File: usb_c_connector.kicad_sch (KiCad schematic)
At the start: 18 parts, among them J5 USB_C_Receptacle_USB2.0_16P, J6 USB_C_Receptacle_USB2.0_16P, U8 USBLC6-2SC6, U9 USBLC6-2SC6

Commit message: Use basic parts where possible
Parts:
- C26, C27, C28, C29, C30, C31: footprint Capacitor_SMD:C_0603_1608Metric_Pad1.08x0.95mm_HandSolder -> Capacitor_SMD:C_0603_1608Metric
- R13, R15, R31, R32: footprint Resistor_SMD:R_0603_1608Metric_Pad0.98x0.95mm_HandSolder -> Resistor_SMD:R_0603_1608Metric; LCSC PN C105580 -> C23186
- R17, R18: footprint Resistor_SMD:R_0603_1608Metric_Pad0.98x0.95mm_HandSolder -> Resistor_SMD:R_0603_1608Metric; LCSC PN C105578 -> C22935
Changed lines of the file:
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@@
 			)
 		)
-		(property "Footprint" "Resistor_SMD:R_0603_1608Metric_Pad0.98x0.95mm_HandSolder"
+		(property "Footprint" "Resistor_SMD:R_0603_1608Metric"
 			(at 86.36 80.518 90)
 			(effects
@@
 			)
 		)
-		(property "LCSC PN" "C105580"
+		(property "LCSC PN" "C23186"
 			(at 86.36 78.74 90)
 			(effects
@@
 			)
 		)
-		(property "Footprint" "Capacitor_SMD:C_0603_1608Metric_Pad1.08x0.95mm_HandSolder"
+		(property "Footprint" "Capacitor_SMD:C_0603_1608Metric"
 			(at 248.6152 78.74 0)
 			(effects
@@
 			)
 		)
-		(property "Footprint" "Resistor_SMD:R_0603_1608Metric_Pad0.98x0.95mm_HandSolder"
+		(property "Footprint" "Resistor_SMD:R_0603_1608Metric"
 			(at 198.12 83.058 90)
 			(effects
@@
 			)
 		)
-		(property "LCSC PN" "C105580"
+		(property "LCSC PN" "C23186"
 			(at 198.12 81.28 90)
 			(effects
@@
 			)
 		)
-		(property "Footprint" "Capacitor_SMD:C_0603_1608Metric_Pad1.08x0.95mm_HandSolder"
+		(property "Footprint" "Capacitor_SMD:C_0603_1608Metric"
 			(at 165.4048 121.92 0)
 			(effects
@@
 			)
 		)
-		(property "Footprint" "Capacitor_SMD:C_0603_1608Metric_Pad1.08x0.95mm_HandSolder"
+		(property "Footprint" "Capacitor_SMD:C_0603_1608Metric"
 			(at 234.6452 78.74 0)
 			(effects
@@
 			)
 		)
-		(property "Footprint" "Resistor_SMD:R_0603_1608Metric_Pad0.98x0.95mm_HandSolder"
+		(property "Footprint" "Resistor_SMD:R_0603_1608Metric"
 			(at 198.12 80.518 90)
 			(effects
@@
 			)
 		)
-		(property "LCSC PN" "C105580"
+		(property "LCSC PN" "C23186"
 			(at 198.12 78.74 90)
 			(effects
@@
 			)
 		)
-		(property "Footprint" "Capacitor_SMD:C_0603_1608Metric_Pad1.08x0.95mm_HandSolder"
+		(property "Footprint" "Capacitor_SMD:C_0603_1608Metric"
 			(at 53.6448 121.92 0)
 			(effects
@@
 			)
 		)
-		(property "Footprint" "Resistor_SMD:R_0603_1608Metric_Pad0.98x0.95mm_HandSolder"
+		(property "Footprint" "Resistor_SMD:R_0603_1608Metric"
 			(at 86.36 83.058 90)
 			(effects
@@
 			)
 		)
-		(property "LCSC PN" "C105580"
+		(property "LCSC PN" "C23186"
 			(at 86.36 81.28 90)
 			(effects
@@
 			)
 		)
-		(property "Footprint" "Resistor_SMD:R_0603_1608Metric_Pad0.98x0.95mm_HandSolder"
+		(property "Footprint" "Resistor_SMD:R_0603_1608Metric"
 			(at 173.228 118.11 90)
 			(effects
@@
 			)
 		)
-		(property "LCSC PN" "C105578"
+		(property "LCSC PN" "C22935"
 			(at 171.45 118.11 0)
 			(effects
@@
 			)
 		)
-		(property "Footprint" "Resistor_SMD:R_0603_1608Metric_Pad0.98x0.95mm_HandSolder"
+		(property "Footprint" "Resistor_SMD:R_0603_1608Metric"
 			(at 61.468 118.11 90)
 			(effects
@@
 			)
 		)
-		(property "LCSC PN" "C105578"
+		(property "LCSC PN" "C22935"
 			(at 59.69 118.11 0)
 			(effects
@@
 			)
 		)
-		(property "Footprint" "Capacitor_SMD:C_0603_1608Metric_Pad1.08x0.95mm_HandSolder"
+		(property "Footprint" "Capacitor_SMD:C_0603_1608Metric"
 			(at 136.8552 78.74 0)
 			(effects
@@
 			)
 		)
-		(property "Footprint" "Capacitor_SMD:C_0603_1608Metric_Pad1.08x0.95mm_HandSolder"
+		(property "Footprint" "Capacitor_SMD:C_0603_1608Metric"
 			(at 122.8852 78.74 0)
 			(effects

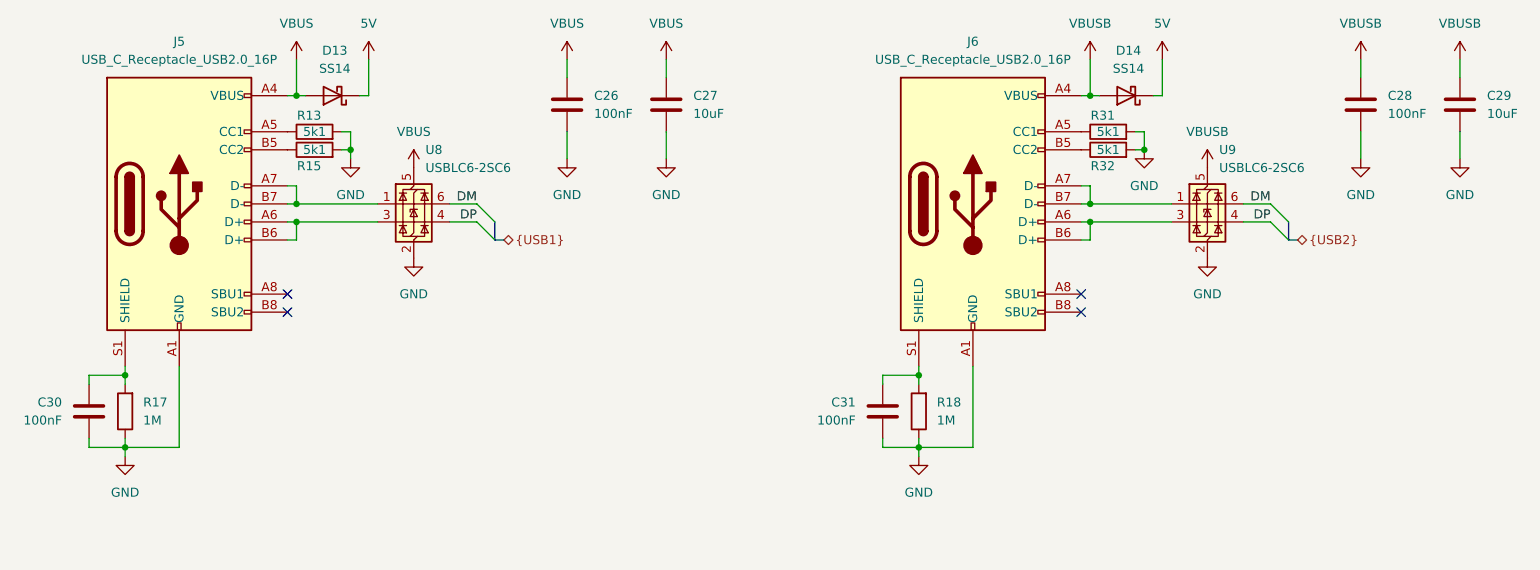
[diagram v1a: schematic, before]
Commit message: Fix bus merging and add net classes
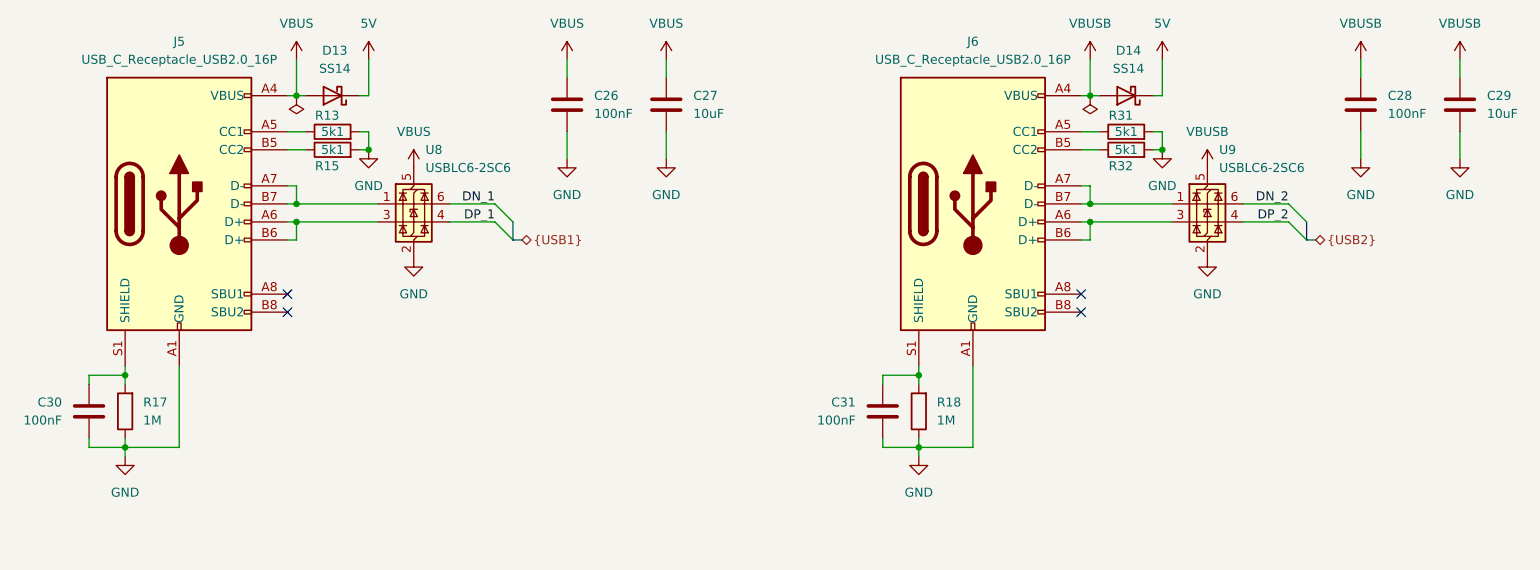
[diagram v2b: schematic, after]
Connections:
- net DM renamed DN_1
- net DN_1: no longer U9.6 (I/O1)
- net DP renamed DP_1
- net DP_1: no longer U9.4 (I/O2)
- new net DN_2: U9.6 (I/O1)
- new net DP_2: U9.4 (I/O2)
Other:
- moved on the sheet: R13, R15, R31, R32

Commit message: Continue layout and update schematic
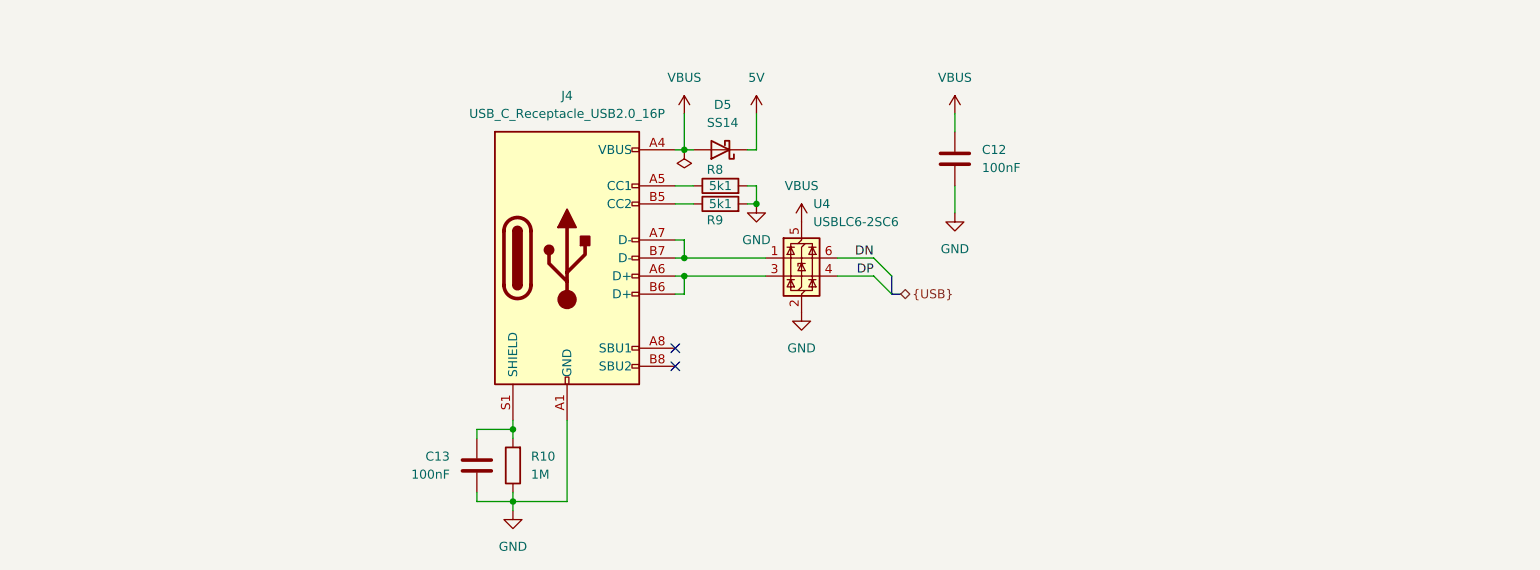
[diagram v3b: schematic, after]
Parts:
- removed C27, C29: 10uF, Capacitor_SMD:C_0603_1608Metric, symbol Device:C
- removed C28, C31: 100nF, Capacitor_SMD:C_0603_1608Metric, symbol Device:C
- removed D14: SS14, Diode_SMD:D_SMA, symbol Diode:SS14
- removed J6: USB_C_Receptacle_USB2.0_16P, Tumbler2:KINGHELM_KH-TYPE-C-16P, symbol Connector:USB_C_Receptacle_USB2.0_16P
- removed R18: 1M, Resistor_SMD:R_0603_1608Metric, symbol Device:R
- removed R31, R32: 5k1, Resistor_SMD:R_0603_1608Metric, symbol Device:R
- removed U9: USBLC6-2SC6, Package_TO_SOT_SMD:SOT-23-6, symbol Power_Protection:USBLC6-2SC6
- renumbered C26 to C12, C30 to C13, D13 to D5, J5 to J4, R17 to R10, R13 to R8, R15 to R9, U8 to U4
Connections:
- net DN_1 renamed DN
- net DP_1 renamed DP
- no-connect marks 4 -> 2
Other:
- moved on the sheet: C12, C13, D5, J4, R10, R8, R9, U4

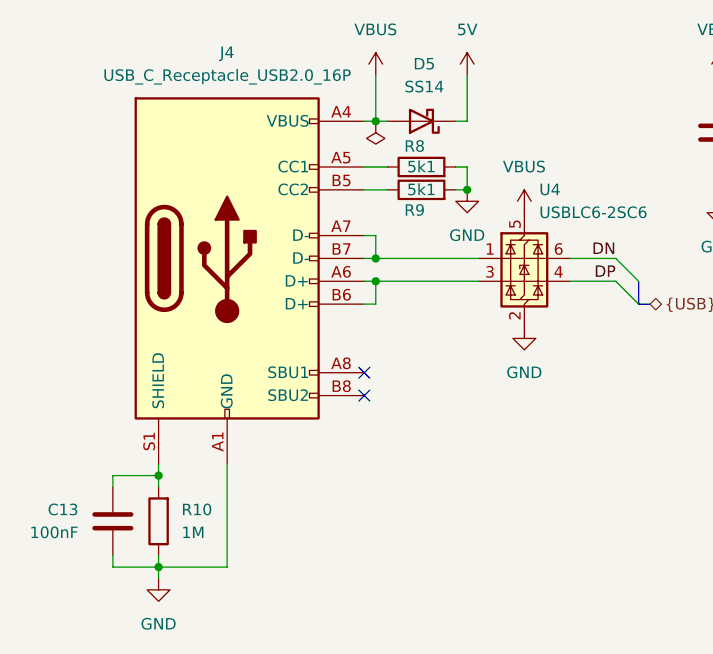
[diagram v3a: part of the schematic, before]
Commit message: Continue layout and add pin header protection
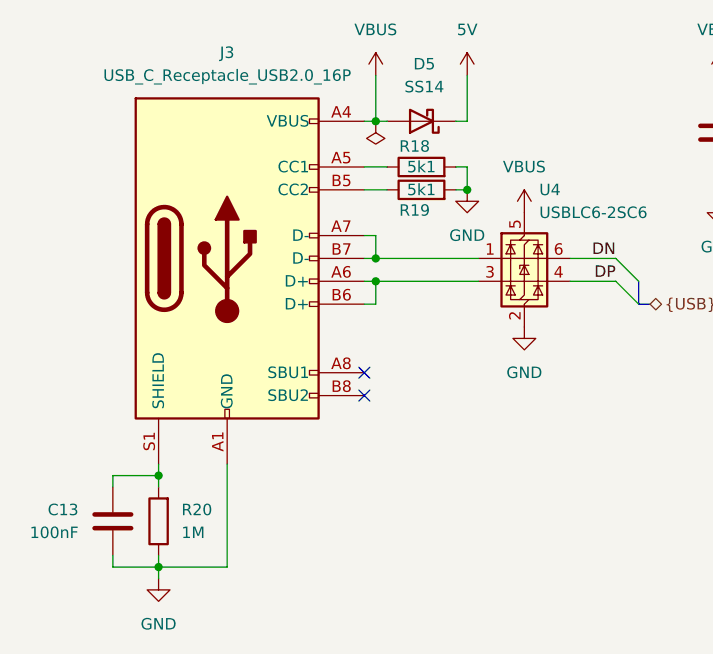
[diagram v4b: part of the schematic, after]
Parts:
- renumbered J4 to J3, R8 to R18, R9 to R19, R10 to R20
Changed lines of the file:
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@@
 		(dnp no)
 		(fields_autoplaced yes)
-		(property "Reference" "#PWR057"
+		(property "Reference" "#PWR053"
 			(at 148.59 80.01 0)
 			(effects
@@
 			(project "Tumbler2_Redesign"
 				(path "/f3fd8d79-9d35-4c04-811e-2697a2740958/84b20f1f-6e00-4937-92e5-6e005c1bde3e"
-					(reference "#PWR057")
+					(reference "#PWR053")
 					(unit 1)
 				)
@@
 			)
 		)
+		(property "Sim.Device" ""
+			(at 154.94 96.52 0)
+			(effects
+				(font
+					(size 1.27 1.27)
+				)
+				(hide yes)
+			)
+		)
 		(pin "5"
 		)
@@
 		(dnp no)
 		(fields_autoplaced yes)
-		(property "Reference" "#PWR056"
+		(property "Reference" "#PWR052"
 			(at 138.43 80.01 0)
 			(effects
@@
 			(project "Tumbler2_Redesign"
 				(path "/f3fd8d79-9d35-4c04-811e-2697a2740958/84b20f1f-6e00-4937-92e5-6e005c1bde3e"
-					(reference "#PWR056")
+					(reference "#PWR052")
 					(unit 1)
 				)
@@
 		(dnp no)
 		(fields_autoplaced yes)
-		(property "Reference" "#PWR061"
+		(property "Reference" "#PWR057"
 			(at 154.94 95.25 0)
 			(effects
@@
 			(project "Tumbler2_Redesign"
 				(path "/f3fd8d79-9d35-4c04-811e-2697a2740958/84b20f1f-6e00-4937-92e5-6e005c1bde3e"
-					(reference "#PWR061")
+					(reference "#PWR057")
 					(unit 1)
 				)
@@
 		(on_board yes)
 		(dnp no)
-		(property "Reference" "R8"
+		(property "Reference" "R18"
 			(at 142.748 84.074 90)
 			(effects
@@
 			)
 		)
+		(property "Sim.Device" ""
+			(at 143.51 86.36 90)
+			(effects
+				(font
+					(size 1.27 1.27)
+				)
+				(hide yes)
+			)
+		)
 		(pin "2"
 		)
@@
 			(project "Tumbler2_Redesign"
 				(path "/f3fd8d79-9d35-4c04-811e-2697a2740958/84b20f1f-6e00-4937-92e5-6e005c1bde3e"
-					(reference "R8")
+					(reference "R18")
 					(unit 1)
 				)
@@
 		(dnp no)
 		(fields_autoplaced yes)
-		(property "Reference" "#PWR063"
+		(property "Reference" "#PWR059"
 			(at 114.3 138.43 0)
 			(effects
@@
 			(project "Tumbler2_Redesign"
 				(path "/f3fd8d79-9d35-4c04-811e-2697a2740958/84b20f1f-6e00-4937-92e5-6e005c1bde3e"
-					(reference "#PWR063")
+					(reference "#PWR059")
 					(unit 1)
 				)
@@
 		(dnp no)
 		(fields_autoplaced yes)
-		(property "Reference" "#PWR060"
+		(property "Reference" "#PWR056"
 			(at 176.53 96.52 0)
 			(effects
@@
 			(project "Tumbler2_Redesign"
 				(path "/f3fd8d79-9d35-4c04-811e-2697a2740958/84b20f1f-6e00-4937-92e5-6e005c1bde3e"
-					(reference "#PWR060")
+					(reference "#PWR056")
 					(unit 1)
 				)
@@
 		(on_board yes)
 		(dnp no)
-		(property "Reference" "J4"
+		(property "Reference" "J3"
 			(at 121.92 73.66 0)
 			(effects
@@
 			)
 		)
+		(property "Sim.Device" ""
+			(at 121.92 96.52 0)
+			(effects
+				(font
+					(size 1.27 1.27)
+				)
+				(hide yes)
+			)
+		)
 		(pin "S1"
 		)
@@
 			(project "Tumbler2_Redesign"
 				(path "/f3fd8d79-9d35-4c04-811e-2697a2740958/84b20f1f-6e00-4937-92e5-6e005c1bde3e"
-					(reference "J4")
+					(reference "J3")
 					(unit 1)
 				)
@@
 			)
 		)
+		(property "Sim.Device" ""
+			(at 109.22 125.73 0)
+			(effects
+				(font
+					(size 1.27 1.27)
+				)
+				(hide yes)
+			)
+		)
 		(pin "2"
 		)
@@
 		(on_board yes)
 		(dnp no)
-		(property "Reference" "R9"
+		(property "Reference" "R19"
 			(at 142.748 91.186 90)
 			(effects
@@
 			)
 		)
+		(property "Sim.Device" ""
+			(at 143.51 88.9 90)
+			(effects
+				(font
+					(size 1.27 1.27)
+				)
+				(hide yes)
+			)
+		)
 		(pin "2"
 		)
@@
 			(project "Tumbler2_Redesign"
 				(path "/f3fd8d79-9d35-4c04-811e-2697a2740958/84b20f1f-6e00-4937-92e5-6e005c1bde3e"
-					(reference "R9")
+					(reference "R19")
 					(unit 1)
 				)
@@
 		(dnp no)
 		(fields_autoplaced yes)
-		(property "Reference" "#PWR058"
+		(property "Reference" "#PWR054"
 			(at 176.53 80.01 0)
 			(effects
@@
 			(project "Tumbler2_Redesign"
 				(path "/f3fd8d79-9d35-4c04-811e-2697a2740958/84b20f1f-6e00-4937-92e5-6e005c1bde3e"
-					(reference "#PWR058")
+					(reference "#PWR054")
 					(unit 1)
 				)
@@
 			)
 		)
+		(property "Sim.Device" ""
+			(at 143.51 81.28 0)
+			(effects
+				(font
+					(size 1.27 1.27)
+				)
+				(hide yes)
+			)
+		)
 		(pin "2"
 		)
@@
 		(dnp no)
 		(fields_autoplaced yes)
-		(property "Reference" "#PWR059"
+		(property "Reference" "#PWR055"
 			(at 148.59 95.25 0)
 			(effects
@@
 			(project "Tumbler2_Redesign"
 				(path "/f3fd8d79-9d35-4c04-811e-2697a2740958/84b20f1f-6e00-4937-92e5-6e005c1bde3e"
-					(reference "#PWR059")
+					(reference "#PWR055")
 					(unit 1)
 				)
@@
 		(dnp no)
 		(fields_autoplaced yes)
-		(property "Reference" "R10"
+		(property "Reference" "R20"
 			(at 116.84 124.4599 0)
 			(effects
@@
 			)
 		)
+		(property "Sim.Device" ""
+			(at 114.3 125.73 0)
+			(effects
+				(font
+					(size 1.27 1.27)
+				)
+				(hide yes)
+			)
+		)
 		(pin "1"
 		)
@@
 			(project "Tumbler2_Redesign"
 				(path "/f3fd8d79-9d35-4c04-811e-2697a2740958/84b20f1f-6e00-4937-92e5-6e005c1bde3e"
-					(reference "R10")
+					(reference "R20")
 					(unit 1)
 				)
@@
 			)
 		)
+		(property "Sim.Device" ""
+			(at 176.53 82.55 0)
+			(effects
+				(font
+					(size 1.27 1.27)
+				)
+				(hide yes)
+			)
+		)
 		(pin "2"
 		)
@@
 		(dnp no)
 		(fields_autoplaced yes)
-		(property "Reference" "#PWR062"
+		(property "Reference" "#PWR058"
 			(at 154.94 110.49 0)
 			(effects
@@
 			(project "Tumbler2_Redesign"
 				(path "/f3fd8d79-9d35-4c04-811e-2697a2740958/84b20f1f-6e00-4937-92e5-6e005c1bde3e"
-					(reference "#PWR062")
-					(unit 1)
-				)
+					(reference "#PWR058")
+					(unit 1)
+				)

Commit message: Document strapping pins
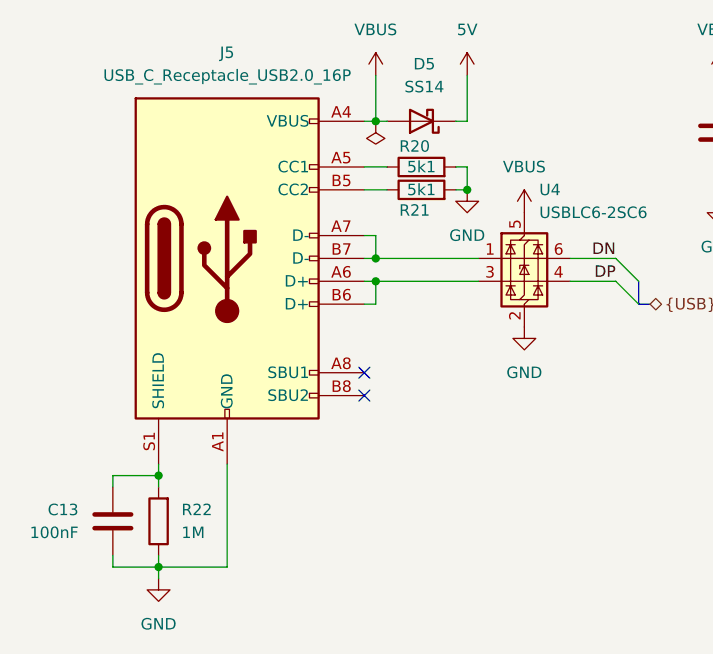
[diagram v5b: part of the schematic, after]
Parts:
- renumbered J3 to J5, R18 to R20, R19 to R21, R20 to R22
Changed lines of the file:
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@@
 		(dnp no)
 		(fields_autoplaced yes)
-		(property "Reference" "#PWR053"
+		(property "Reference" "#PWR058"
 			(at 148.59 80.01 0)
 			(effects
@@
 			(project "Tumbler2_Redesign"
 				(path "/f3fd8d79-9d35-4c04-811e-2697a2740958/84b20f1f-6e00-4937-92e5-6e005c1bde3e"
-					(reference "#PWR053")
+					(reference "#PWR058")
 					(unit 1)
 				)
@@
 		(dnp no)
 		(fields_autoplaced yes)
-		(property "Reference" "#PWR052"
+		(property "Reference" "#PWR057"
 			(at 138.43 80.01 0)
 			(effects
@@
 			(project "Tumbler2_Redesign"
 				(path "/f3fd8d79-9d35-4c04-811e-2697a2740958/84b20f1f-6e00-4937-92e5-6e005c1bde3e"
-					(reference "#PWR052")
+					(reference "#PWR057")
 					(unit 1)
 				)
@@
 		(dnp no)
 		(fields_autoplaced yes)
-		(property "Reference" "#PWR057"
+		(property "Reference" "#PWR062"
 			(at 154.94 95.25 0)
 			(effects
@@
 			(project "Tumbler2_Redesign"
 				(path "/f3fd8d79-9d35-4c04-811e-2697a2740958/84b20f1f-6e00-4937-92e5-6e005c1bde3e"
-					(reference "#PWR057")
+					(reference "#PWR062")
 					(unit 1)
 				)
@@
 		(on_board yes)
 		(dnp no)
-		(property "Reference" "R18"
+		(property "Reference" "R20"
 			(at 142.748 84.074 90)
 			(effects
@@
 			(project "Tumbler2_Redesign"
 				(path "/f3fd8d79-9d35-4c04-811e-2697a2740958/84b20f1f-6e00-4937-92e5-6e005c1bde3e"
-					(reference "R18")
+					(reference "R20")
 					(unit 1)
 				)
@@
 		(dnp no)
 		(fields_autoplaced yes)
-		(property "Reference" "#PWR059"
+		(property "Reference" "#PWR064"
 			(at 114.3 138.43 0)
 			(effects
@@
 			(project "Tumbler2_Redesign"
 				(path "/f3fd8d79-9d35-4c04-811e-2697a2740958/84b20f1f-6e00-4937-92e5-6e005c1bde3e"
-					(reference "#PWR059")
+					(reference "#PWR064")
 					(unit 1)
 				)
@@
 		(dnp no)
 		(fields_autoplaced yes)
-		(property "Reference" "#PWR056"
+		(property "Reference" "#PWR061"
 			(at 176.53 96.52 0)
 			(effects
@@
 			(project "Tumbler2_Redesign"
 				(path "/f3fd8d79-9d35-4c04-811e-2697a2740958/84b20f1f-6e00-4937-92e5-6e005c1bde3e"
-					(reference "#PWR056")
+					(reference "#PWR061")
 					(unit 1)
 				)
@@
 		(on_board yes)
 		(dnp no)
-		(property "Reference" "J3"
+		(property "Reference" "J5"
 			(at 121.92 73.66 0)
 			(effects
@@
 			(project "Tumbler2_Redesign"
 				(path "/f3fd8d79-9d35-4c04-811e-2697a2740958/84b20f1f-6e00-4937-92e5-6e005c1bde3e"
-					(reference "J3")
+					(reference "J5")
 					(unit 1)
 				)
@@
 		(on_board yes)
 		(dnp no)
-		(property "Reference" "R19"
+		(property "Reference" "R21"
 			(at 142.748 91.186 90)
 			(effects
@@
 			(project "Tumbler2_Redesign"
 				(path "/f3fd8d79-9d35-4c04-811e-2697a2740958/84b20f1f-6e00-4937-92e5-6e005c1bde3e"
-					(reference "R19")
+					(reference "R21")
 					(unit 1)
 				)
@@
 		(dnp no)
 		(fields_autoplaced yes)
-		(property "Reference" "#PWR054"
+		(property "Reference" "#PWR059"
 			(at 176.53 80.01 0)
 			(effects
@@
 			(project "Tumbler2_Redesign"
 				(path "/f3fd8d79-9d35-4c04-811e-2697a2740958/84b20f1f-6e00-4937-92e5-6e005c1bde3e"
-					(reference "#PWR054")
+					(reference "#PWR059")
 					(unit 1)
 				)
@@
 		(dnp no)
 		(fields_autoplaced yes)
-		(property "Reference" "#PWR055"
+		(property "Reference" "#PWR060"
 			(at 148.59 95.25 0)
 			(effects
@@
 			(project "Tumbler2_Redesign"
 				(path "/f3fd8d79-9d35-4c04-811e-2697a2740958/84b20f1f-6e00-4937-92e5-6e005c1bde3e"
-					(reference "#PWR055")
+					(reference "#PWR060")
 					(unit 1)
 				)
@@
 		(dnp no)
 		(fields_autoplaced yes)
-		(property "Reference" "R20"
+		(property "Reference" "R22"
 			(at 116.84 124.4599 0)
 			(effects
@@
 			(project "Tumbler2_Redesign"
 				(path "/f3fd8d79-9d35-4c04-811e-2697a2740958/84b20f1f-6e00-4937-92e5-6e005c1bde3e"
-					(reference "R20")
+					(reference "R22")
 					(unit 1)
 				)
@@
 		(dnp no)
 		(fields_autoplaced yes)
-		(property "Reference" "#PWR058"
+		(property "Reference" "#PWR063"
 			(at 154.94 110.49 0)
 			(effects
@@
 			(project "Tumbler2_Redesign"
 				(path "/f3fd8d79-9d35-4c04-811e-2697a2740958/84b20f1f-6e00-4937-92e5-6e005c1bde3e"
-					(reference "#PWR058")
-					(unit 1)
-				)
+					(reference "#PWR063")
+					(unit 1)
+				)
